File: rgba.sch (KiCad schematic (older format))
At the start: 74 parts, among them J1 CHARGE CONN, J11 Screw 1, J12 Screw 1, J2 BATT CONN, J3 UART_GND, J4 R SPK OUT, J5 L SPK OUT, J6 UART_TX, J7 UART_VBUS, J8 UART_RX, SW1 Switch_RA, SW2 Switch_RA, SW3 Switch_RA, U1 FSC-BT806, U2 PCM5242, U3 TPS62849DLCR, U4 TPS7A3501, U5 TPS65133DPD, U6 OPA1662

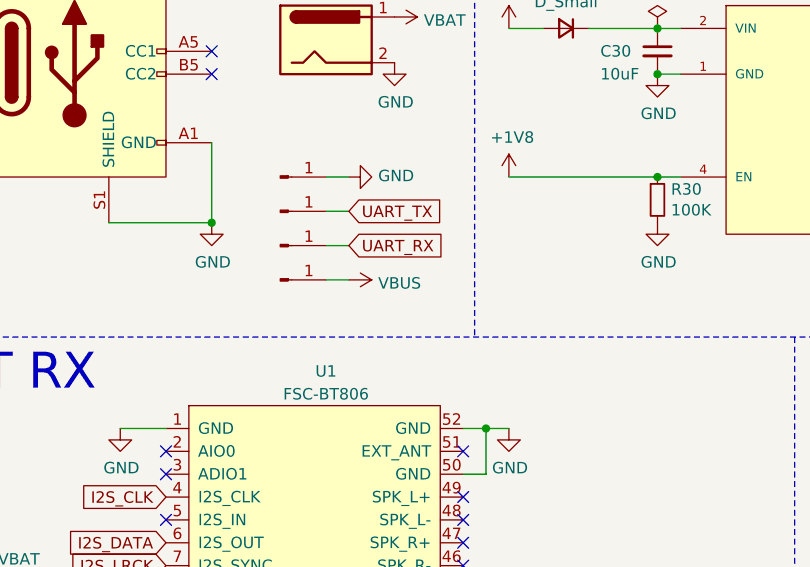
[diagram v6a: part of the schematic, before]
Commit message: connect programming header power to 3v3 instead of vbus
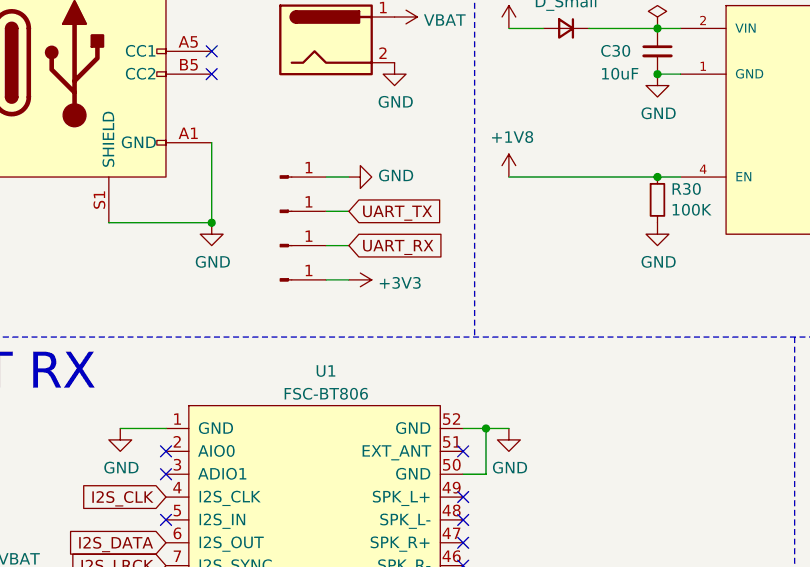
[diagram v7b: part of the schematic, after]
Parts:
- J3, J6, J7, J8: footprint TestPoint:TestPoint_THTPad_D1.5mm_Drill0.7mm -> rgba:TestPoint_THTPad_D1.5mm_Drill0.7mm
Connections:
- net +3V3: now also J7.1 (Pin_1)
- net VBUS: no longer J7.1 (Pin_1)
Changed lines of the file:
@@
-	0    1    1    0
-$EndComp
-$Comp
-L power:VBUS #PWR0158
-U 1 1 60DC8673
-P 2300 2250
-F 0 "#PWR0158" H 2300 2100 50  0001 C CNN
-F 1 "VBUS" V 2315 2378 50  0000 L CNN
-F 2 "" H 2300 2250 50  0001 C CNN
-F 3 "" H 2300 2250 50  0001 C CNN
-	1    2300 2250
 	0    1    1    0
 $EndComp
@@
 F 0 "J3" H 2108 1889 50  0001 C CNN
 F 1 "UART_GND" H 2108 1890 50  0001 C CNN
-F 2 "TestPoint:TestPoint_THTPad_D1.5mm_Drill0.7mm" H 2000 1800 50  0001 C CNN
+F 2 "rgba:TestPoint_THTPad_D1.5mm_Drill0.7mm" H 2000 1800 50  0001 C CNN
 F 3 "~" H 2000 1800 50  0001 C CNN
 	1    2000 1800
@@
 F 0 "J7" H 2108 2339 50  0001 C CNN
 F 1 "UART_VBUS" H 2108 2340 50  0001 C CNN
-F 2 "TestPoint:TestPoint_THTPad_D1.5mm_Drill0.7mm" H 2000 2250 50  0001 C CNN
+F 2 "rgba:TestPoint_THTPad_D1.5mm_Drill0.7mm" H 2000 2250 50  0001 C CNN
 F 3 "~" H 2000 2250 50  0001 C CNN
 	1    2000 2250
@@
 F 0 "J8" H 2108 2189 50  0001 C CNN
 F 1 "UART_RX" H 2108 2190 50  0001 C CNN
-F 2 "TestPoint:TestPoint_THTPad_D1.5mm_Drill0.7mm" H 2000 2100 50  0001 C CNN
+F 2 "rgba:TestPoint_THTPad_D1.5mm_Drill0.7mm" H 2000 2100 50  0001 C CNN
 F 3 "~" H 2000 2100 50  0001 C CNN
 	1    2000 2100
@@
 F 0 "J6" H 2108 2039 50  0001 C CNN
 F 1 "UART_TX" H 2108 2040 50  0001 C CNN
-F 2 "TestPoint:TestPoint_THTPad_D1.5mm_Drill0.7mm" H 2000 1950 50  0001 C CNN
+F 2 "rgba:TestPoint_THTPad_D1.5mm_Drill0.7mm" H 2000 1950 50  0001 C CNN
 F 3 "~" H 2000 1950 50  0001 C CNN
 	1    2000 1950
@@
 NoConn ~ 1500 4400
 NoConn ~ 1500 4300
+$Comp
+L power:+3V3 #PWR?
+U 1 1 606A0E8E
+P 2300 2250
+F 0 "#PWR?" H 2300 2100 50  0001 C CNN
+F 1 "+3V3" V 2315 2378 50  0000 L CNN
+F 2 "" H 2300 2250 50  0001 C CNN
+F 3 "" H 2300 2250 50  0001 C CNN
+	1    2300 2250
+	0    1    1    0
+$EndComp
 $EndSCHEMATC

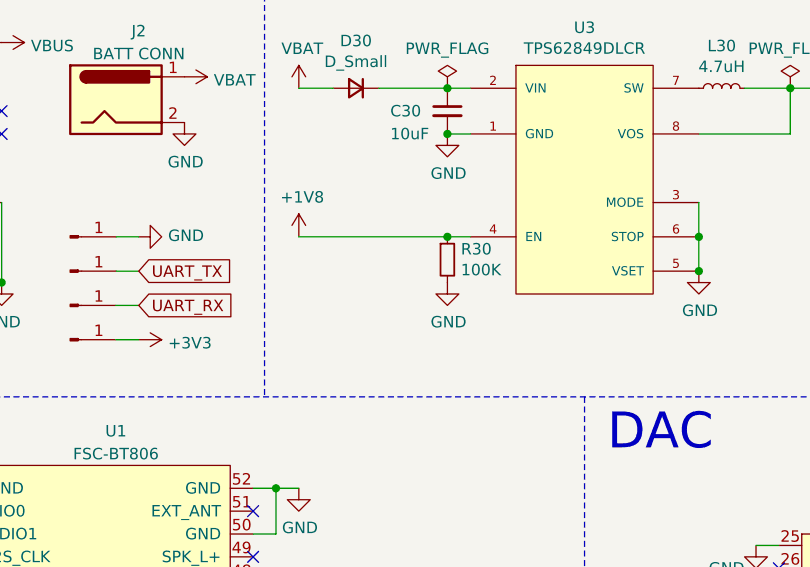
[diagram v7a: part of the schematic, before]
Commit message: remove TPS62849 enable pin pulldown resistor because it has an internal pulldown resistor
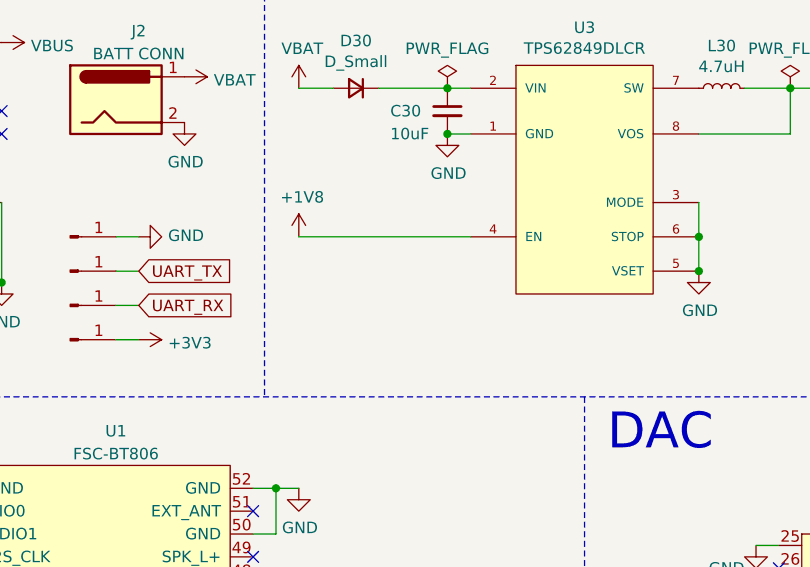
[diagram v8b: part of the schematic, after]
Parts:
- removed R30: 100K, Resistor_SMD:R_0402_1005Metric_Pad0.72x0.64mm_HandSolder, symbol Device:R_Small
